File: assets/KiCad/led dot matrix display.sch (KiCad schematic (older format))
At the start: 33 parts

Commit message: minor update
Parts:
- removed Q? (x16): PN2222A, Package_TO_SOT_THT:TO-92_Inline, symbol Transistor_BJT:PN2222A
- removed R? (x16): 330, symbol Device:R
- removed U?: HD14514BP, symbol MyICs:HD14514BP

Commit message: minor update
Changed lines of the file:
@@
 $Descr A4 11693 8268
 encoding utf-8
-Sheet 1 5
+Sheet 1 8
 Title "test"
 Date ""
@@
 $EndDescr
 $Sheet
-S 7350 1550 2000 2000
-U 5F5984FE
-F0 "driver" 50
-F1 "driver.sch" 50
-F2 "D1" I R 9350 3050 50
-F3 "D2" I R 9350 3150 50
-F4 "D3" I R 9350 3250 50
-F5 "D4" I R 9350 3350 50
-F6 "LED0" O L 7350 1750 50
-F7 "LED1" O L 7350 1850 50
-F8 "LED2" O L 7350 1950 50
-F9 "LED3" O L 7350 2050 50
-F10 "LED4" O L 7350 2150 50
-F11 "LED5" O L 7350 2250 50
-F12 "LED6" O L 7350 2350 50
-F13 "LED7" O L 7350 2450 50
-F14 "LED8" O L 7350 2650 50
-F15 "LED9" O L 7350 2750 50
-F16 "LED10" O L 7350 2850 50
-F17 "LED11" O L 7350 2950 50
-F18 "LED12" O L 7350 3050 50
-F19 "LED13" O L 7350 3150 50
-F20 "LED14" O L 7350 3250 50
-F21 "LED15" O L 7350 3350 50
+S 4850 1000 2000 3500
+U 5F54EEE0
+F0 "led matrix" 50
+F1 "led matrix.sch" 50
+F2 "C0" O R 6850 4350 50
+F3 "C1" O R 6850 4250 50
+F4 "C2" O R 6850 4150 50
+F5 "C3" O R 6850 4050 50
+F6 "C4" O R 6850 3950 50
+F7 "C5" O R 6850 3850 50
+F8 "C6" O R 6850 3750 50
+F9 "C7" O R 6850 3650 50
+F10 "C8" O R 6850 3550 50
+F11 "C9" O R 6850 3450 50
+F12 "C10" O R 6850 3350 50
+F13 "C11" O R 6850 3250 50
+F14 "C12" O R 6850 3150 50
+F15 "C13" O R 6850 3050 50
+F16 "C14" O R 6850 2950 50
+F17 "C15" O R 6850 2850 50
+F18 "DA0" I L 4850 4350 50
+F19 "DA1" I L 4850 4250 50
+F20 "DA2" I L 4850 4150 50
+F21 "DA3" I L 4850 4050 50
+F22 "DA4" I L 4850 3950 50
+F23 "DA5" I L 4850 3850 50
+F24 "DA6" I L 4850 3750 50
+F25 "DA7" I L 4850 3650 50
+F26 "DB0" I L 4850 2650 50
+F27 "DB1" I L 4850 2550 50
+F28 "DB2" I L 4850 2450 50
+F29 "DB3" I L 4850 2350 50
+F30 "DB4" I L 4850 2250 50
+F31 "DB5" I L 4850 2150 50
+F32 "DB6" I L 4850 2050 50
+F33 "DB7" I L 4850 1950 50
+F34 "DA8" I L 4850 3550 50
+F35 "DA9" I L 4850 3450 50
+F36 "DA10" I L 4850 3350 50
+F37 "DA11" I L 4850 3250 50
+F38 "DA12" I L 4850 3150 50
+F39 "DA13" I L 4850 3050 50
+F40 "DA14" I L 4850 2950 50
+F41 "DA15" I L 4850 2850 50
+F42 "DB8" I L 4850 1850 50
+F43 "DB9" I L 4850 1750 50
+F44 "DB10" I L 4850 1650 50
+F45 "DB11" I L 4850 1550 50
+F46 "DB12" I L 4850 1450 50
+F47 "DB13" I L 4850 1350 50
+F48 "DB14" I L 4850 1250 50
+F49 "DB15" I L 4850 1150 50
 $EndSheet
 $Sheet
-S 4300 4350 3500 1500
-U 5F5AB140
+S 7850 2500 2000 2000
+U 5F5A0E48
 F0 "controller" 50
 F1 "controller.sch" 50
 $EndSheet
 $Sheet
-S 3750 1600 2000 2000
-U 5F54EEE0
-F0 "led matrix" 50
-F1 "led matrix.sch" 50
+S 1850 1000 2000 3500
+U 5F5984FE
+F0 "driver" 50
+F1 "driver.sch" 50
+F2 "D1" I L 1850 4350 50
+F3 "D2" I L 1850 4250 50
+F4 "D3" I L 1850 4150 50
+F5 "D4" I L 1850 4050 50
+F6 "LA0" O R 3850 4350 50
+F7 "LA1" O R 3850 4250 50
+F8 "LA2" O R 3850 4150 50
+F9 "LA3" O R 3850 4050 50
+F10 "LA4" O R 3850 3950 50
+F11 "LA5" O R 3850 3850 50
+F12 "LA6" O R 3850 3750 50
+F13 "LA7" O R 3850 3650 50
+F14 "LA8" O R 3850 3550 50
+F15 "LA9" O R 3850 3450 50
+F16 "LA10" O R 3850 3350 50
+F17 "LA11" O R 3850 3250 50
+F18 "LA12" O R 3850 3150 50
+F19 "LA13" O R 3850 3050 50
+F20 "LA14" O R 3850 2950 50
+F21 "LA15" O R 3850 2850 50
+F22 "LB0" O R 3850 2650 50
+F23 "LB1" O R 3850 2550 50
+F24 "LB2" O R 3850 2450 50
+F25 "LB3" O R 3850 2350 50
+F26 "LB4" O R 3850 2250 50
+F27 "LB5" O R 3850 2150 50
+F28 "LB6" O R 3850 2050 50
+F29 "LB7" O R 3850 1950 50
+F30 "LB8" O R 3850 1850 50
+F31 "LB9" O R 3850 1750 50
+F32 "LB10" O R 3850 1650 50
+F33 "LB11" O R 3850 1550 50
+F34 "LB12" O R 3850 1450 50
+F35 "LB13" O R 3850 1350 50
+F36 "LB14" O R 3850 1250 50
+F37 "LB15" O R 3850 1150 50
 $EndSheet
+Wire Wire Line
+	3850 4350 4850 4350
+Wire Wire Line
+	3850 4250 4850 4250
+Wire Wire Line
+	3850 4150 4850 4150
+Wire Wire Line
+	3850 4050 4850 4050
+Wire Wire Line
+	3850 3950 4850 3950
+Wire Wire Line
+	3850 3850 4850 3850
+Wire Wire Line
+	3850 3750 4850 3750
+Wire Wire Line
+	3850 3650 4850 3650
+Wire Wire Line
+	3850 3550 4850 3550
+Wire Wire Line
+	3850 3450 4850 3450
+Wire Wire Line
+	3850 3350 4850 3350
+Wire Wire Line
+	3850 3250 4850 3250
+Wire Wire Line
+	3850 3150 4850 3150
+Wire Wire Line
+	3850 3050 4850 3050
+Wire Wire Line
+	3850 2950 4850 2950
+Wire Wire Line
+	3850 2850 4850 2850
+Wire Wire Line
+	3850 2650 4850 2650
+Wire Wire Line
+	3850 2550 4850 2550
+Wire Wire Line
+	3850 2450 4850 2450
+Wire Wire Line
+	3850 2350 4850 2350
+Wire Wire Line
+	3850 2250 4850 2250
+Wire Wire Line
+	3850 2150 4850 2150
+Wire Wire Line
+	3850 2050 4850 2050
+Wire Wire Line
+	3850 1950 4850 1950
+Wire Wire Line
+	3850 1850 4850 1850
+Wire Wire Line
+	3850 1750 4850 1750
+Wire Wire Line
+	3850 1650 4850 1650
+Wire Wire Line
+	3850 1550 4850 1550
+Wire Wire Line
+	3850 1450 4850 1450
+Wire Wire Line
+	3850 1350 4850 1350
+Wire Wire Line
+	3850 1250 4850 1250
+Wire Wire Line
+	3850 1150 4850 1150
 $EndSCHEMATC

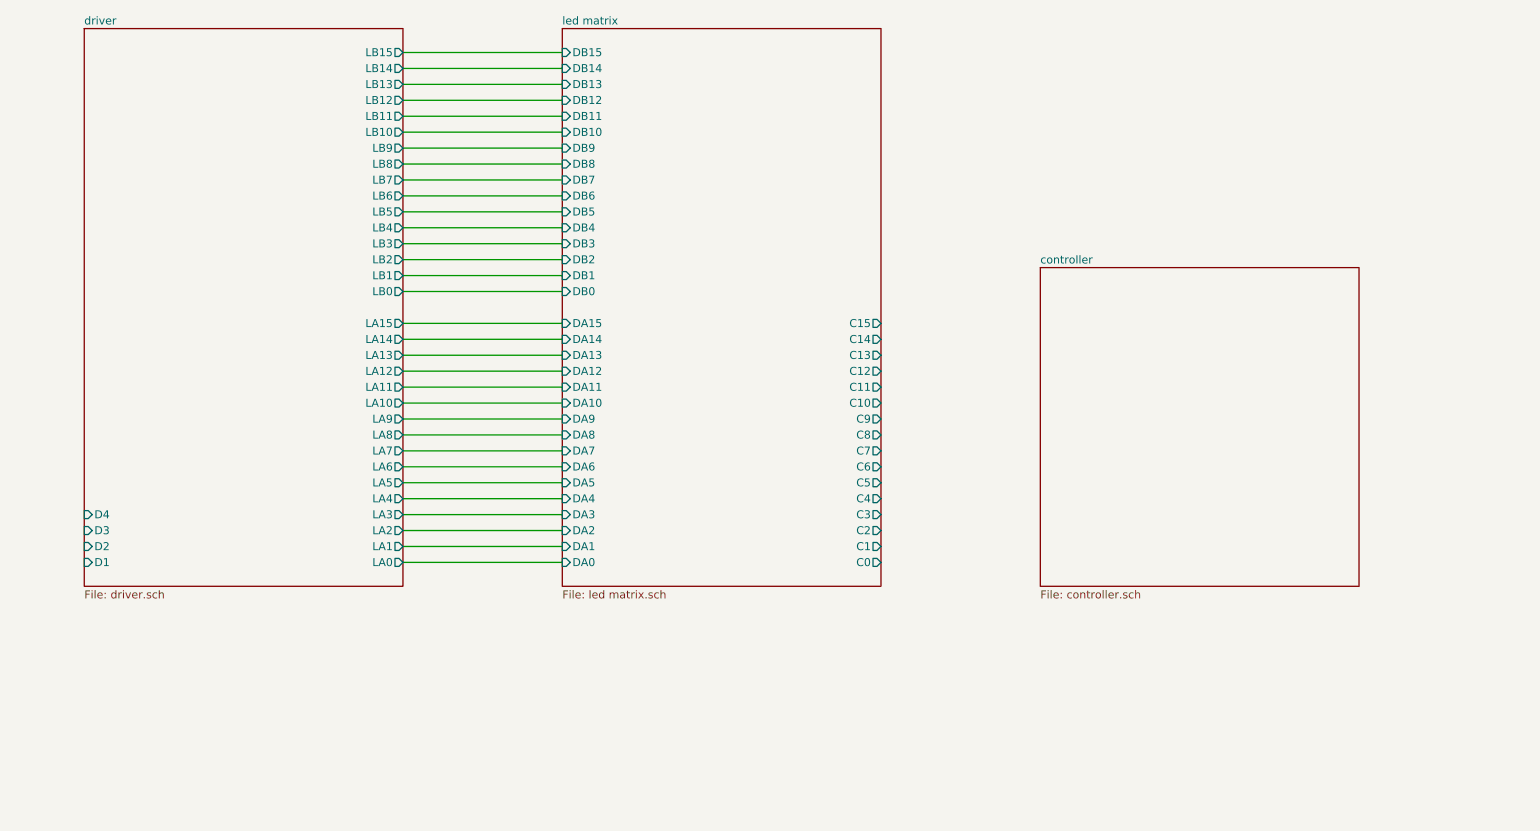
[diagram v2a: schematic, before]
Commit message: update schematic
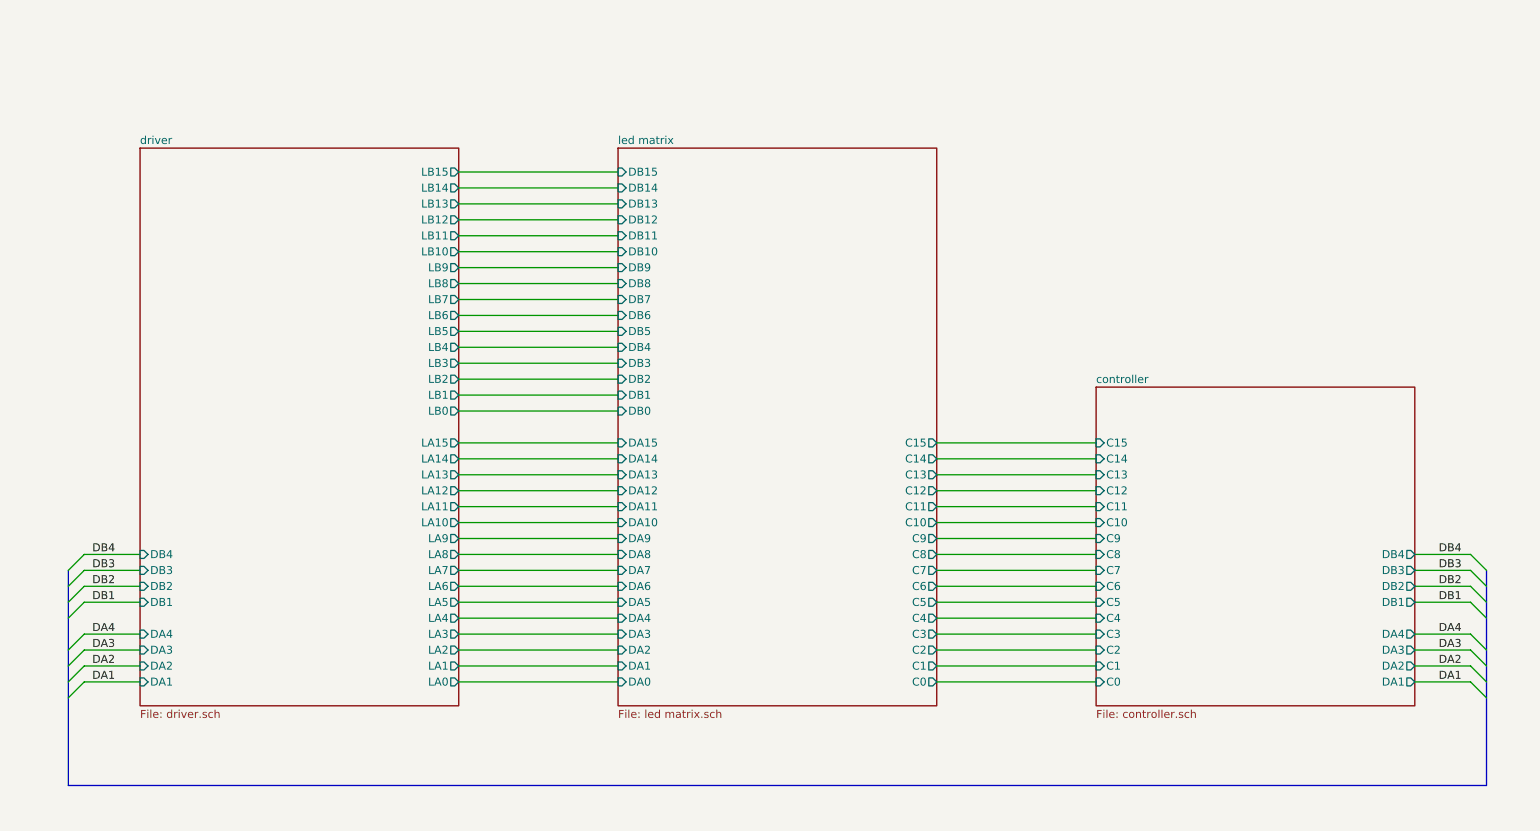
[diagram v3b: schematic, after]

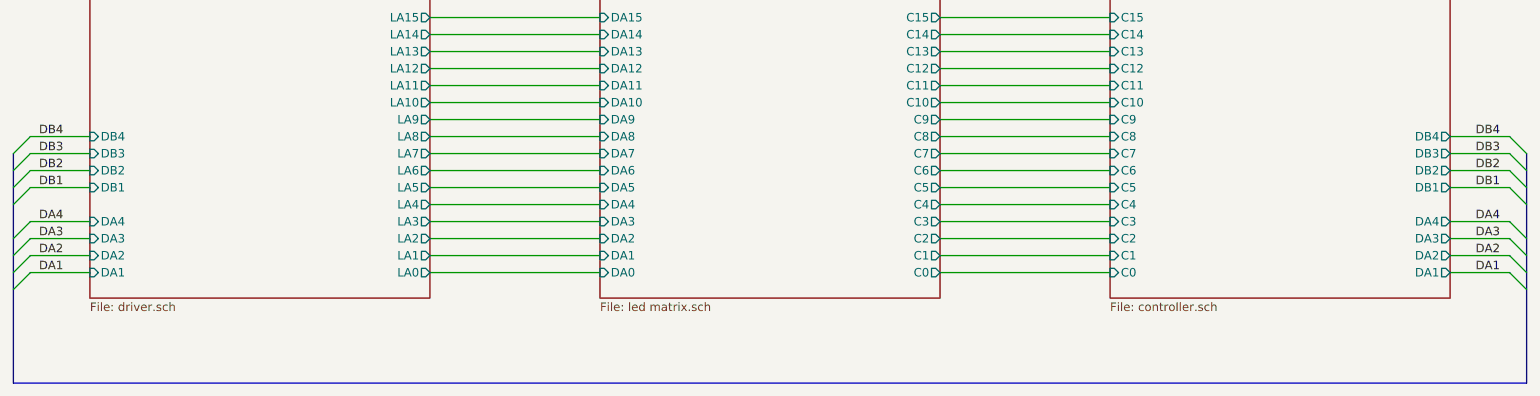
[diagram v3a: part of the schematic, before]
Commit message: schematic update
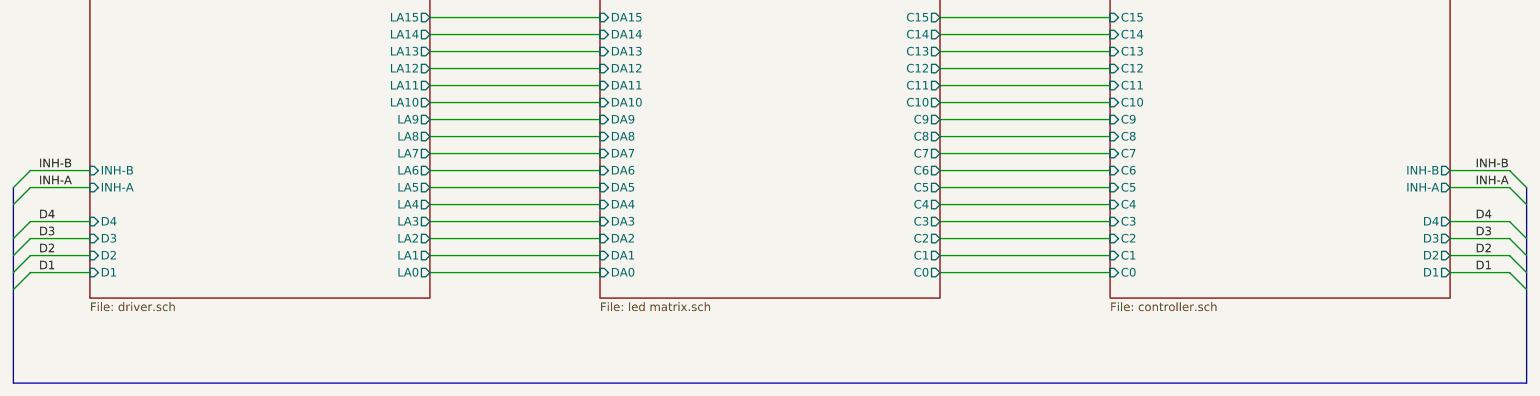
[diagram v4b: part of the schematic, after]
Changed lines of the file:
@@
 F0 "controller" 50
 F1 "controller.sch" 50
-F2 "DA1" O R 10200 5100 50
-F3 "DA2" O R 10200 5000 50
-F4 "DA3" O R 10200 4900 50
-F5 "DA4" O R 10200 4800 50
-F6 "DB1" O R 10200 4600 50
-F7 "DB2" O R 10200 4500 50
-F8 "DB3" O R 10200 4400 50
-F9 "DB4" O R 10200 4300 50
-F10 "C0" I L 8200 5100 50
-F11 "C1" I L 8200 5000 50
-F12 "C2" I L 8200 4900 50
-F13 "C3" I L 8200 4800 50
-F14 "C4" I L 8200 4700 50
-F15 "C5" I L 8200 4600 50
-F16 "C6" I L 8200 4500 50
-F17 "C7" I L 8200 4400 50
-F18 "C8" I L 8200 4300 50
-F19 "C9" I L 8200 4200 50
-F20 "C10" I L 8200 4100 50
-F21 "C11" I L 8200 4000 50
-F22 "C12" I L 8200 3900 50
-F23 "C13" I L 8200 3800 50
-F24 "C14" I L 8200 3700 50
-F25 "C15" I L 8200 3600 50
+F2 "D1" O R 10200 5100 50
+F3 "D2" O R 10200 5000 50
+F4 "D3" O R 10200 4900 50
+F5 "D4" O R 10200 4800 50
+F6 "C0" I L 8200 5100 50
+F7 "C1" I L 8200 5000 50
+F8 "C2" I L 8200 4900 50
+F9 "C3" I L 8200 4800 50
+F10 "C4" I L 8200 4700 50
+F11 "C5" I L 8200 4600 50
+F12 "C6" I L 8200 4500 50
+F13 "C7" I L 8200 4400 50
+F14 "C8" I L 8200 4300 50
+F15 "C9" I L 8200 4200 50
+F16 "C10" I L 8200 4100 50
+F17 "C11" I L 8200 4000 50
+F18 "C12" I L 8200 3900 50
+F19 "C13" I L 8200 3800 50
+F20 "C14" I L 8200 3700 50
+F21 "C15" I L 8200 3600 50
+F22 "INH-A" O R 10200 4600 50
+F23 "INH-B" O R 10200 4500 50
 $EndSheet
+Wire Wire Line
+	4200 5100 5200 5100
+Wire Wire Line
+	4200 5000 5200 5000
+Wire Wire Line
+	4200 4900 5200 4900
+Wire Wire Line
+	4200 4800 5200 4800
+Wire Wire Line
+	4200 4700 5200 4700
+Wire Wire Line
+	4200 4600 5200 4600
+Wire Wire Line
+	4200 4500 5200 4500
+Wire Wire Line
+	4200 4400 5200 4400
+Wire Wire Line
+	4200 4300 5200 4300
+Wire Wire Line
+	4200 4200 5200 4200
+Wire Wire Line
+	4200 4100 5200 4100
+Wire Wire Line
+	4200 4000 5200 4000
+Wire Wire Line
+	4200 3900 5200 3900
+Wire Wire Line
+	4200 3800 5200 3800
+Wire Wire Line
+	4200 3700 5200 3700
+Wire Wire Line
+	4200 3600 5200 3600
+Wire Wire Line
+	4200 3400 5200 3400
+Wire Wire Line
+	4200 3300 5200 3300
+Wire Wire Line
+	4200 3200 5200 3200
+Wire Wire Line
+	4200 3100 5200 3100
+Wire Wire Line
+	4200 3000 5200 3000
+Wire Wire Line
+	4200 2900 5200 2900
+Wire Wire Line
+	4200 2800 5200 2800
+Wire Wire Line
+	4200 2700 5200 2700
+Wire Wire Line
+	4200 2600 5200 2600
+Wire Wire Line
+	4200 2500 5200 2500
+Wire Wire Line
+	4200 2400 5200 2400
+Wire Wire Line
+	4200 2300 5200 2300
+Wire Wire Line
+	4200 2200 5200 2200
+Wire Wire Line
+	4200 2100 5200 2100
+Wire Wire Line
+	4200 2000 5200 2000
+Wire Wire Line
+	4200 1900 5200 1900
+Wire Wire Line
+	7200 3600 8200 3600
+Wire Wire Line
+	7200 3700 8200 3700
+Wire Wire Line
+	7200 3800 8200 3800
+Wire Wire Line
+	7200 3900 8200 3900
+Wire Wire Line
+	7200 4000 8200 4000
+Wire Wire Line
+	7200 4100 8200 4100
+Wire Wire Line
+	7200 4200 8200 4200
+Wire Wire Line
+	7200 4300 8200 4300
+Wire Wire Line
+	7200 4400 8200 4400
+Wire Wire Line
+	7200 4500 8200 4500
+Wire Wire Line
+	7200 4600 8200 4600
+Wire Wire Line
+	7200 4700 8200 4700
+Wire Wire Line
+	7200 4800 8200 4800
+Wire Wire Line
+	7200 4900 8200 4900
+Wire Wire Line
+	7200 5000 8200 5000
+Wire Wire Line
+	7200 5100 8200 5100
+Wire Wire Line
+	2200 4800 1850 4800
+Wire Wire Line
+	2200 4900 1850 4900
+Wire Wire Line
+	2200 5000 1850 5000
+Wire Wire Line
+	2200 5100 1850 5100
+Entry Wire Line
+	1750 4900 1850 4800
+Entry Wire Line
+	1750 5000 1850 4900
+Entry Wire Line
+	1750 5100 1850 5000
+Entry Wire Line
+	1750 5200 1850 5100
+Wire Wire Line
+	10550 4500 10200 4500
+Wire Wire Line
+	10550 4600 10200 4600
+Wire Wire Line
+	10550 4800 10200 4800
+Wire Wire Line
+	10550 4900 10200 4900
+Wire Wire Line
+	10550 5000 10200 5000
+Wire Wire Line
+	10550 5100 10200 5100
+Entry Wire Line
+	10550 4500 10650 4600
+Entry Wire Line
+	10550 4600 10650 4700
+Entry Wire Line
+	10550 4800 10650 4900
+Entry Wire Line
+	10550 4900 10650 5000
+Entry Wire Line
+	10550 5000 10650 5100
+Entry Wire Line
+	10550 5100 10650 5200
+Wire Bus Line
+	10650 5750 1750 5750
+Text Label 1900 5100 0    50   ~ 0
+D1
+Text Label 1900 5000 0    50   ~ 0
+D2
+Text Label 1900 4900 0    50   ~ 0
+D3
+Text Label 1900 4800 0    50   ~ 0
+D4
+Text Label 10350 4600 0    50   ~ 0
+INH-A
+Text Label 10350 5100 0    50   ~ 0
+D1
+Text Label 10350 5000 0    50   ~ 0
+D2
+Text Label 10350 4900 0    50   ~ 0
+D3
+Text Label 10350 4800 0    50   ~ 0
+D4
+Wire Wire Line
+	2200 4500 1850 4500
+Wire Wire Line
+	1850 4600 2200 4600
+Text Label 1900 4500 0    50   ~ 0
+INH-B
+Text Label 1900 4600 0    50   ~ 0
+INH-A
 $Sheet
 S 2200 1750 2000 3500
@@
 F32 "LB14" O R 4200 2000 50
 F33 "LB15" O R 4200 1900 50
-F34 "DA1" I L 2200 5100 50
-F35 "DA2" I L 2200 5000 50
-F36 "DA3" I L 2200 4900 50
-F37 "DA4" I L 2200 4800 50
-F38 "DB1" I L 2200 4600 50
-F39 "DB2" I L 2200 4500 50
-F40 "DB3" I L 2200 4400 50
-F41 "DB4" I L 2200 4300 50
+F34 "D1" I L 2200 5100 50
+F35 "D2" I L 2200 5000 50
+F36 "D3" I L 2200 4900 50
+F37 "D4" I L 2200 4800 50
+F38 "INH-A" I L 2200 4600 50
+F39 "INH-B" I L 2200 4500 50
 $EndSheet
-Wire Wire Line
-	4200 5100 5200 5100
-Wire Wire Line
-	4200 5000 5200 5000
-Wire Wire Line
-	4200 4900 5200 4900
-Wire Wire Line
-	4200 4800 5200 4800
-Wire Wire Line
-	4200 4700 5200 4700
-Wire Wire Line
-	4200 4600 5200 4600
-Wire Wire Line
-	4200 4500 5200 4500
-Wire Wire Line
-	4200 4400 5200 4400
-Wire Wire Line
-	4200 4300 5200 4300
-Wire Wire Line
-	4200 4200 5200 4200
-Wire Wire Line
-	4200 4100 5200 4100
-Wire Wire Line
-	4200 4000 5200 4000
-Wire Wire Line
-	4200 3900 5200 3900
-Wire Wire Line
-	4200 3800 5200 3800
-Wire Wire Line
-	4200 3700 5200 3700
-Wire Wire Line
-	4200 3600 5200 3600
-Wire Wire Line
-	4200 3400 5200 3400
-Wire Wire Line
-	4200 3300 5200 3300
-Wire Wire Line
-	4200 3200 5200 3200
-Wire Wire Line
-	4200 3100 5200 3100
-Wire Wire Line
-	4200 3000 5200 3000
-Wire Wire Line
-	4200 2900 5200 2900
-Wire Wire Line
-	4200 2800 5200 2800
-Wire Wire Line
-	4200 2700 5200 2700
-Wire Wire Line
-	4200 2600 5200 2600
-Wire Wire Line
-	4200 2500 5200 2500
-Wire Wire Line
-	4200 2400 5200 2400
-Wire Wire Line
-	4200 2300 5200 2300
-Wire Wire Line
-	4200 2200 5200 2200
-Wire Wire Line
-	4200 2100 5200 2100
-Wire Wire Line
-	4200 2000 5200 2000
-Wire Wire Line
-	4200 1900 5200 1900
-Wire Wire Line
-	7200 3600 8200 3600
-Wire Wire Line
-	7200 3700 8200 3700
-Wire Wire Line
-	7200 3800 8200 3800
-Wire Wire Line
-	7200 3900 8200 3900
-Wire Wire Line
-	7200 4000 8200 4000
-Wire Wire Line
-	7200 4100 8200 4100
-Wire Wire Line
-	7200 4200 8200 4200
-Wire Wire Line
-	7200 4300 8200 4300
-Wire Wire Line
-	7200 4400 8200 4400
-Wire Wire Line
-	7200 4500 8200 4500
-Wire Wire Line
-	7200 4600 8200 4600
-Wire Wire Line
-	7200 4700 8200 4700
-Wire Wire Line
-	7200 4800 8200 4800
-Wire Wire Line
-	7200 4900 8200 4900
-Wire Wire Line
-	7200 5000 8200 5000
-Wire Wire Line
-	7200 5100 8200 5100
-Wire Wire Line
-	2200 4300 1850 4300
-Wire Wire Line
-	2200 4400 1850 4400
-Wire Wire Line
-	2200 4500 1850 4500
-Wire Wire Line
-	2200 4600 1850 4600
-Wire Wire Line
-	2200 4800 1850 4800
-Wire Wire Line
-	2200 4900 1850 4900
-Wire Wire Line
-	2200 5000 1850 5000
-Wire Wire Line
-	2200 5100 1850 5100
-Entry Wire Line
-	1750 4400 1850 4300
-Entry Wire Line
-	1750 4500 1850 4400
 Entry Wire Line
 	1750 4600 1850 4500
 Entry Wire Line
 	1750 4700 1850 4600
-Entry Wire Line
-	1750 4900 1850 4800
-Entry Wire Line
-	1750 5000 1850 4900
-Entry Wire Line
-	1750 5100 1850 5000
-Entry Wire Line
-	1750 5200 1850 5100
-Wire Wire Line
-	10200 4300 10550 4300
-Wire Wire Line
-	10550 4400 10200 4400
-Wire Wire Line
-	10550 4500 10200 4500
-Wire Wire Line
-	10550 4600 10200 4600
-Wire Wire Line
-	10550 4800 10200 4800
-Wire Wire Line
-	10550 4900 10200 4900
-Wire Wire Line
-	10550 5000 10200 5000
-Wire Wire Line
-	10550 5100 10200 5100
-Entry Wire Line
-	10550 4300 10650 4400
-Entry Wire Line
-	10550 4400 10650 4500
-Entry Wire Line
-	10550 4500 10650 4600
-Entry Wire Line
-	10550 4600 10650 4700
-Entry Wire Line
-	10550 4800 10650 4900
-Entry Wire Line
-	10550 4900 10650 5000
-Entry Wire Line
-	10550 5000 10650 5100
-Entry Wire Line
-	10550 5100 10650 5200
+Text Label 10350 4500 0    50   ~ 0
+INH-B
 Wire Bus Line
-	10650 5750 1750 5750
-Text Label 1900 5100 0    50   ~ 0
-DA1
-Text Label 1900 5000 0    50   ~ 0
-DA2
-Text Label 1900 4900 0    50   ~ 0
-DA3
-Text Label 1900 4800 0    50   ~ 0
-DA4
-Text Label 1900 4600 0    50   ~ 0
-DB1
-Text Label 1900 4500 0    50   ~ 0
-DB2
-Text Label 1900 4400 0    50   ~ 0
-DB3
-Text Label 1900 4300 0    50   ~ 0
-DB4
-Text Label 10350 4600 0    50   ~ 0
-DB1
-Text Label 10350 4500 0    50   ~ 0
-DB2
-Text Label 10350 4400 0    50   ~ 0
-DB3
-Text Label 10350 4300 0    50   ~ 0
-DB4
-Text Label 10350 5100 0    50   ~ 0
-DA1
-Text Label 10350 5000 0    50   ~ 0
-DA2
-Text Label 10350 4900 0    50   ~ 0
-DA3
-Text Label 10350 4800 0    50   ~ 0
-DA4
+	1750 4600 1750 5750
 Wire Bus Line
-	10650 4400 10650 5750
-Wire Bus Line
-	1750 4400 1750 5750
+	10650 4600 10650 5750
 $EndSCHEMATC
